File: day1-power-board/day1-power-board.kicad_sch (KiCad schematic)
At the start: 0 parts

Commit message: Complete power supply schematic
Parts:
- added C1: 0.33uF, symbol Device:C
- added C2: 10uF, symbol Device:C
- added C3: 0.1uF, symbol Device:C
- added C4: 33uF, symbol Device:C
- added D1: 1N4007, Diode_THT:D_DO-41_SOD81_P10.16mm_Horizontal, symbol Diode:1N4007
- added D2: LED, symbol Device:LED
- added J1: V_IN, symbol Connector:Screw_Terminal_01x02
- added J2: V_OUT, symbol Connector:Screw_Terminal_01x02
- added R1: 620, symbol Device:R
- added U1: L78L05_SOT89, Package_TO_SOT_SMD:SOT-89-3, symbol Regulator_Linear:L78L05_SOT89
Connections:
- new net: D2.1 (K), R1.1
- new net +5V: C3.1, C4.1, D2.2 (A), J2.1 (Pin_1), U1.1 (OUT)
- new net 12V_PROT: C1.1, C2.1, D1.1 (K), U1.3 (IN)
- new net 12V_RAW: D1.2 (A), J1.2 (Pin_2)
- new net GND: C1.2, C2.2, C3.2, C4.2, J1.1 (Pin_1), J2.2 (Pin_2), R1.2, U1.2 (GND)

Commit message: Complete PCB layout and routing
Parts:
- C1, C2, C3, C4: footprint (none) -> Capacitor_SMD:C_0805_2012Metric
- D2: footprint (none) -> LED_SMD:LED_0603_1608Metric
- J1, J2: footprint (none) -> TerminalBlock_Phoenix:TerminalBlock_Phoenix_MKDS-1,5-2-5.08_1x02_P5.08mm_Horizontal
- R1: footprint (none) -> Resistor_SMD:R_0805_2012Metric
- U1: footprint Package_TO_SOT_SMD:SOT-89-3 -> Package_TO_SOT_THT:TO-220-3_Vertical
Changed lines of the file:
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@@
 			)
 		)
-		(property "Footprint" ""
+		(property "Footprint" "Capacitor_SMD:C_0805_2012Metric"
 			(at 126.6952 82.55 0)
 			(effects
@@
 			)
 		)
-		(property "Footprint" ""
+		(property "Footprint" "TerminalBlock_Phoenix:TerminalBlock_Phoenix_MKDS-1,5-2-5.08_1x02_P5.08mm_Horizontal"
 			(at 223.52 64.77 0)
 			(effects
@@
 			)
 		)
-		(property "Footprint" ""
+		(property "Footprint" "Capacitor_SMD:C_0805_2012Metric"
 			(at 190.1952 83.82 0)
 			(effects
@@
 			)
 		)
-		(property "Footprint" ""
+		(property "Footprint" "Capacitor_SMD:C_0805_2012Metric"
 			(at 173.6852 83.82 0)
 			(effects
@@
 			)
 		)
-		(property "Footprint" ""
+		(property "Footprint" "TerminalBlock_Phoenix:TerminalBlock_Phoenix_MKDS-1,5-2-5.08_1x02_P5.08mm_Horizontal"
 			(at 83.82 67.31 0)
 			(effects
@@
 			)
 		)
-		(property "Footprint" ""
+		(property "Footprint" "Capacitor_SMD:C_0805_2012Metric"
 			(at 141.9352 82.55 0)
 			(effects
@@
 			)
 		)
-		(property "Footprint" ""
+		(property "Footprint" "Resistor_SMD:R_0805_2012Metric"
 			(at 201.422 80.01 90)
 			(effects
@@
 			)
 		)
-		(property "Footprint" ""
+		(property "Footprint" "LED_SMD:LED_0603_1608Metric"
 			(at 203.2 69.85 0)
 			(effects
@@
 			)
 		)
-		(property "Footprint" "Package_TO_SOT_SMD:SOT-89-3"
+		(property "Footprint" "Package_TO_SOT_THT:TO-220-3_Vertical"
 			(at 157.48 59.69 0)
 			(effects

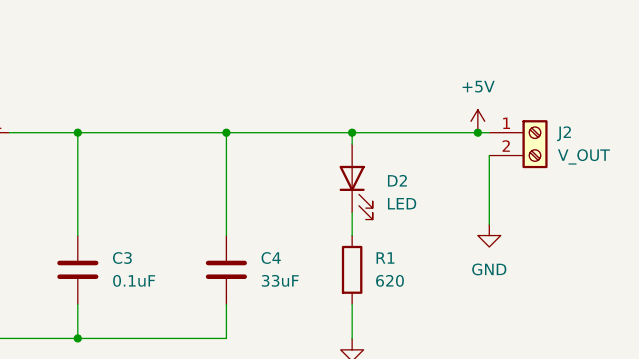
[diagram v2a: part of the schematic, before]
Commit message: Add 5V test point
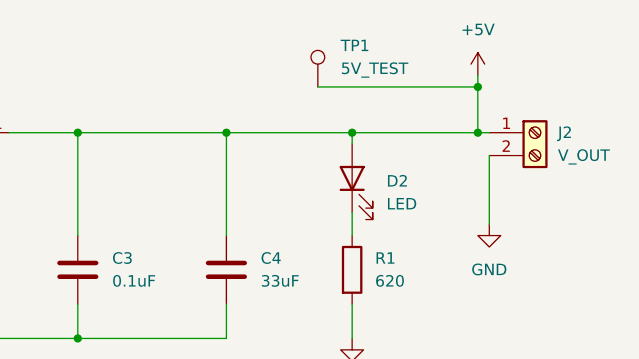
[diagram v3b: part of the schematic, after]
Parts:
- added TP1: 5V_TEST, TestPoint:TestPoint_Pad_2.0x2.0mm, symbol Connector:TestPoint
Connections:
- net +5V: now also TP1.1
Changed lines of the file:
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@@
+	)
+	(junction
+		(at 217.17 59.69)
+		(diameter 0)
+		(color 0 0 0 0)
 	)
 	(junction
@@
 	(wire
 		(pts
+			(xy 199.39 59.69) (xy 217.17 59.69)
+		)
+		(stroke
+			(width 0)
+			(type default)
+		)
+	)
+	(wire
+		(pts
 			(xy 140.97 64.77) (xy 143.51 64.77)
 		)
@@
 	(wire
 		(pts
+			(xy 217.17 59.69) (xy 217.17 64.77)
+		)
+		(stroke
+			(width 0)
+			(type default)
+		)
+	)
+	(wire
+		(pts
 			(xy 172.72 64.77) (xy 172.72 76.2)
 		)
@@
 		(pts
 			(xy 88.9 64.77) (xy 97.79 64.77)
+		)
+		(stroke
+			(width 0)
+			(type default)
+		)
+	)
+	(wire
+		(pts
+			(xy 217.17 58.42) (xy 217.17 59.69)
 		)
 		(stroke
@@
 	)
 	(symbol
+		(lib_id "Connector:TestPoint")
+		(at 199.39 59.69 0)
+		(unit 1)
+		(exclude_from_sim no)
+		(in_bom yes)
+		(on_board yes)
+		(dnp no)
+		(fields_autoplaced yes)
+		(property "Reference" "TP1"
+			(at 201.93 55.1179 0)
+			(effects
+				(font
+					(size 1.27 1.27)
+				)
+				(justify left)
+			)
+		)
+		(property "Value" "5V_TEST"
+			(at 201.93 57.6579 0)
+			(effects
+				(font
+					(size 1.27 1.27)
+				)
+				(justify left)
+			)
+		)
+		(property "Footprint" "TestPoint:TestPoint_Pad_2.0x2.0mm"
+			(at 204.47 59.69 0)
+			(effects
+				(font
+					(size 1.27 1.27)
+				)
+				(hide yes)
+			)
+		)
+		(property "Datasheet" "~"
+			(at 204.47 59.69 0)
+			(effects
+				(font
+					(size 1.27 1.27)
+				)
+				(hide yes)
+			)
+		)
+		(property "Description" "test point"
+			(at 199.39 59.69 0)
+			(effects
+				(font
+					(size 1.27 1.27)
+				)
+				(hide yes)
+			)
+		)
+		(pin "1"
+		)
+		(instances
+			(project ""
+				(path "/36a2fab3-956e-472e-853f-9772f700f857"
+					(reference "TP1")
+					(unit 1)
+				)
+			)
+		)
+	)
+	(symbol
 		(lib_id "Device:C")
 		(at 125.73 78.74 0)
@@
 	(symbol
 		(lib_id "power:+5V")
-		(at 217.17 64.77 0)
+		(at 217.17 58.42 0)
 		(unit 1)
 		(exclude_from_sim no)
@@
 		(fields_autoplaced yes)
 		(property "Reference" "#PWR05"
-			(at 217.17 68.58 0)
+			(at 217.17 62.23 0)
 			(effects
 				(font
@@
 		)
 		(property "Value" "+5V"
-			(at 217.17 59.69 0)
+			(at 217.17 53.34 0)
 			(effects
 				(font
@@
 		)
 		(property "Footprint" ""
-			(at 217.17 64.77 0)
+			(at 217.17 58.42 0)
 			(effects
 				(font
@@
 		)
 		(property "Datasheet" ""
-			(at 217.17 64.77 0)
+			(at 217.17 58.42 0)
 			(effects
 				(font
@@
 		)
 		(property "Description" "Power symbol creates a global label with name \"+5V\""
-			(at 217.17 64.77 0)
-			(effects
-				(font
+			(at 217.17 58.42 0)
+			(effects
+				(font

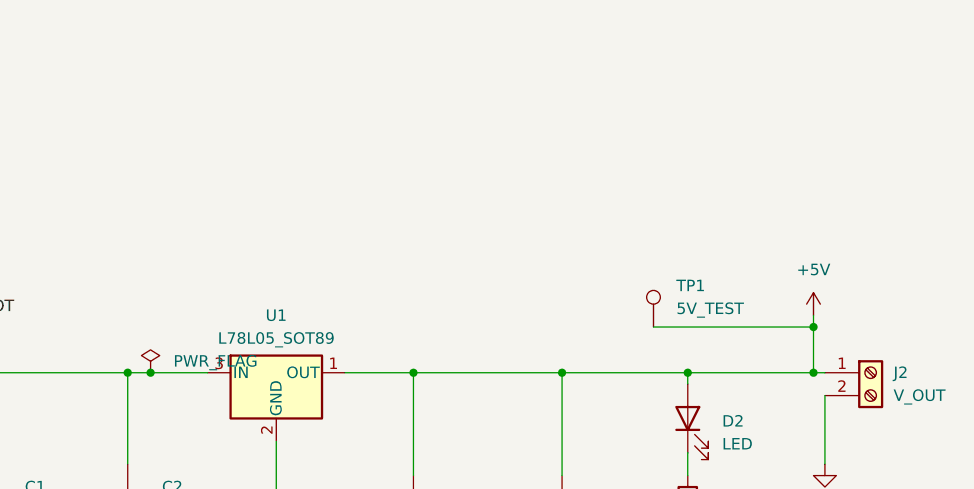
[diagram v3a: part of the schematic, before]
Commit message: Add custom sensor footprint
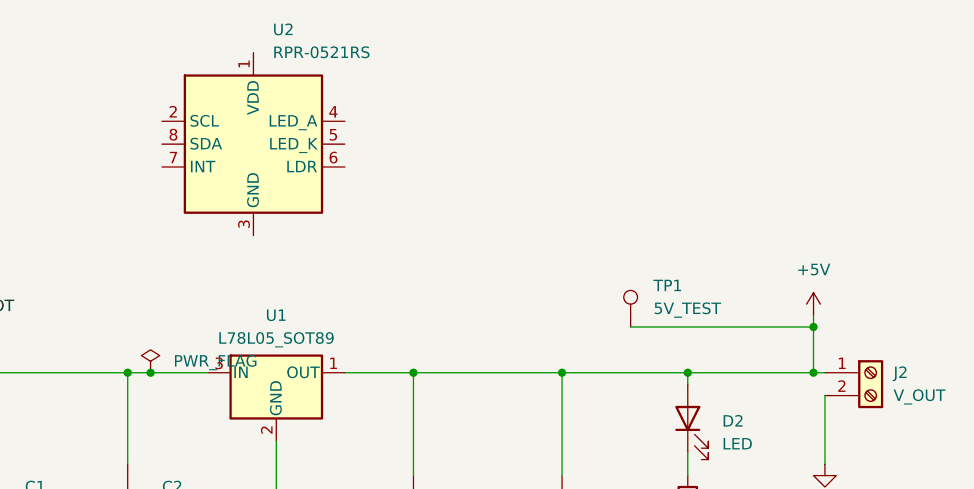
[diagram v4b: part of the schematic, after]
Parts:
- added U2: RPR-0521RS, MYLIBRARY:MY_SENSOR_1x04_P2.54mm, symbol Sensor:RPR-0521RS
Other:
- moved on the sheet: TP1
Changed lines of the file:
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@@
 	(wire
 		(pts
-			(xy 199.39 59.69) (xy 217.17 59.69)
+			(xy 196.85 59.69) (xy 217.17 59.69)
 		)
 		(stroke
@@
 	(symbol
 		(lib_id "Connector:TestPoint")
-		(at 199.39 59.69 0)
+		(at 196.85 59.69 0)
 		(unit 1)
 		(exclude_from_sim no)
@@
 		(fields_autoplaced yes)
 		(property "Reference" "TP1"
-			(at 201.93 55.1179 0)
+			(at 199.39 55.1179 0)
 			(effects
 				(font
@@
 		)
 		(property "Value" "5V_TEST"
-			(at 201.93 57.6579 0)
+			(at 199.39 57.6579 0)
 			(effects
 				(font
@@
 		)
 		(property "Footprint" "TestPoint:TestPoint_Pad_2.0x2.0mm"
-			(at 204.47 59.69 0)
+			(at 201.93 59.69 0)
 			(effects
 				(font
@@
 		)
 		(property "Datasheet" "~"
-			(at 204.47 59.69 0)
+			(at 201.93 59.69 0)
 			(effects
 				(font
@@
 		)
 		(property "Description" "test point"
-			(at 199.39 59.69 0)
+			(at 196.85 59.69 0)
 			(effects
 				(font
@@
 					(unit 1)
 				)
+			)
+		)
+	)
+	(symbol
+		(lib_id "Sensor:RPR-0521RS")
+		(at 154.94 39.37 0)
+		(unit 1)
+		(exclude_from_sim no)
+		(in_bom yes)
+		(on_board yes)
+		(dnp no)
+		(fields_autoplaced yes)
+		(property "Reference" "U2"
+			(at 157.0833 26.67 0)
+			(effects
+				(font
+					(size 1.27 1.27)
+				)
+				(justify left)
+			)
+		)
+		(property "Value" "RPR-0521RS"
+			(at 157.0833 29.21 0)
+			(effects
+				(font
+					(size 1.27 1.27)
+				)
+				(justify left)
+			)
+		)
+		(property "Footprint" "MYLIBRARY:MY_SENSOR_1x04_P2.54mm"
+			(at 154.94 33.401 0)
+			(effects
+				(font
+					(size 1.27 1.27)
+				)
+				(hide yes)
+			)
+		)
+		(property "Datasheet" "https://fscdn.rohm.com/en/products/databook/datasheet/opto/optical_sensor/opto_module/rpr-0521rs-e.pdf"
+			(at 155.067 45.593 0)
+			(effects
+				(font
+					(size 1.27 1.27)
+				)
+				(hide yes)
+			)
+		)
+		(property "Description" "Digital Proximity and Ambient Light Sensor"
+			(at 154.94 39.37 0)
+			(effects
+				(font
+					(size 1.27 1.27)
+				)
+				(hide yes)
+			)
+		)
+		(pin "2"
+		)
+		(pin "4"
+		)
+		(pin "1"
+		)
+		(pin "5"
+		)
+		(pin "7"
+		)
+		(pin "8"
+		)
+		(pin "6"
+		)
+		(pin "3"
+		)
+		(instances
+			(project ""
+				(path "/36a2fab3-956e-472e-853f-9772f700f857"
+					(reference "U2")
+					(unit 1)
+				)

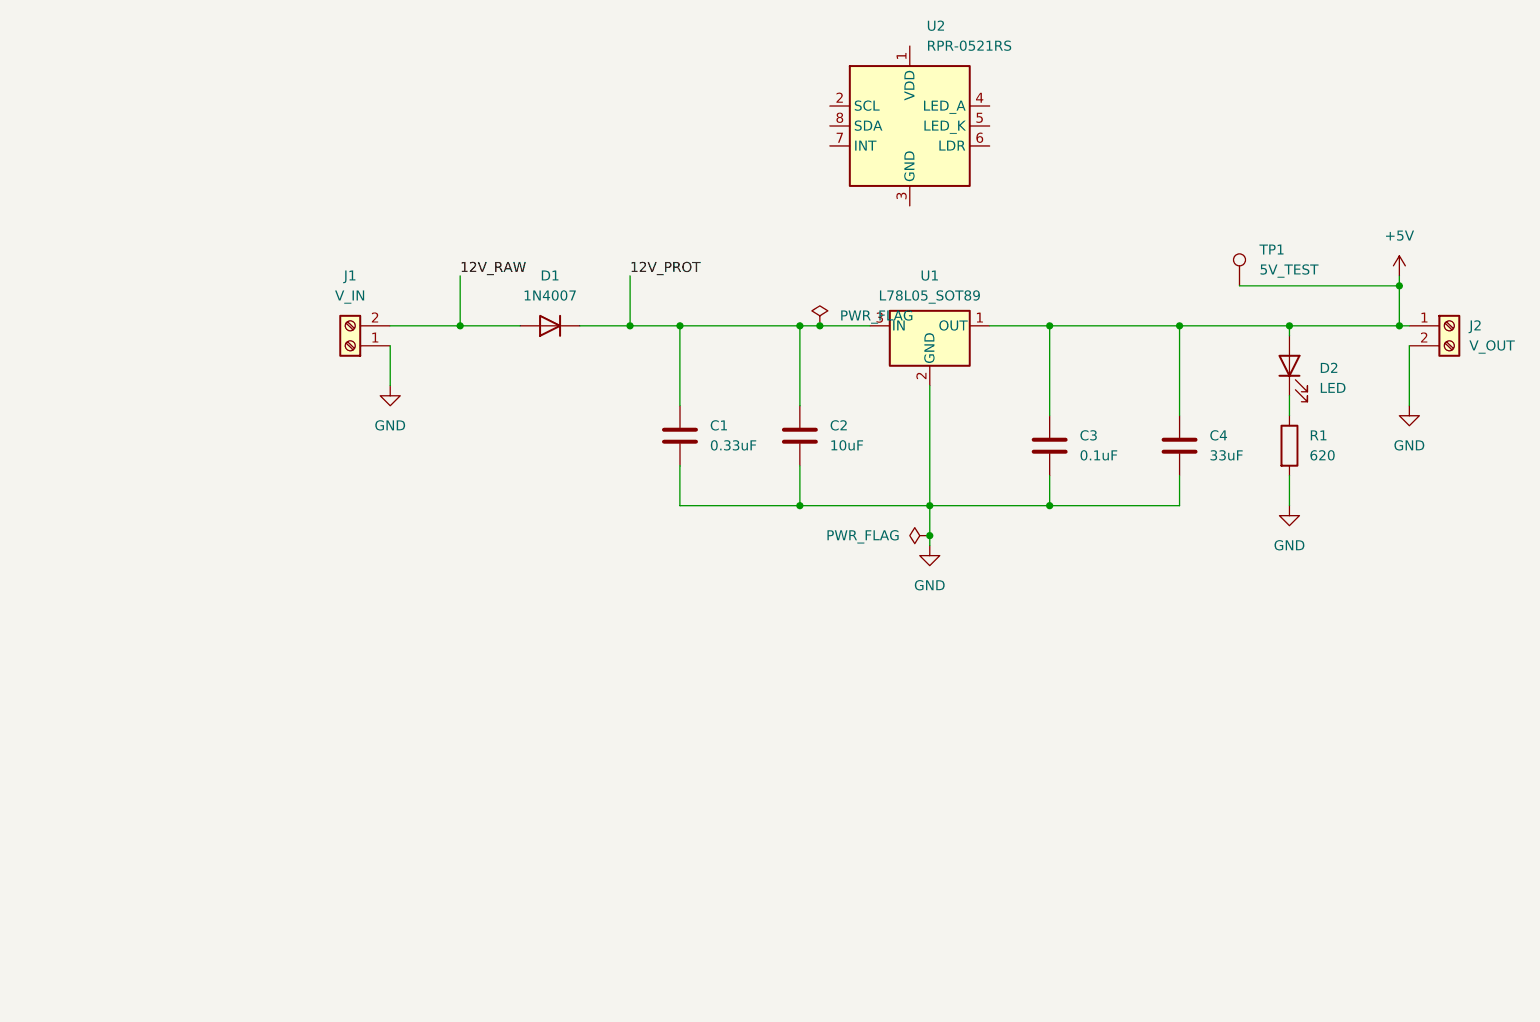
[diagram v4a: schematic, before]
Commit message: Add hierarchical label for power circuit
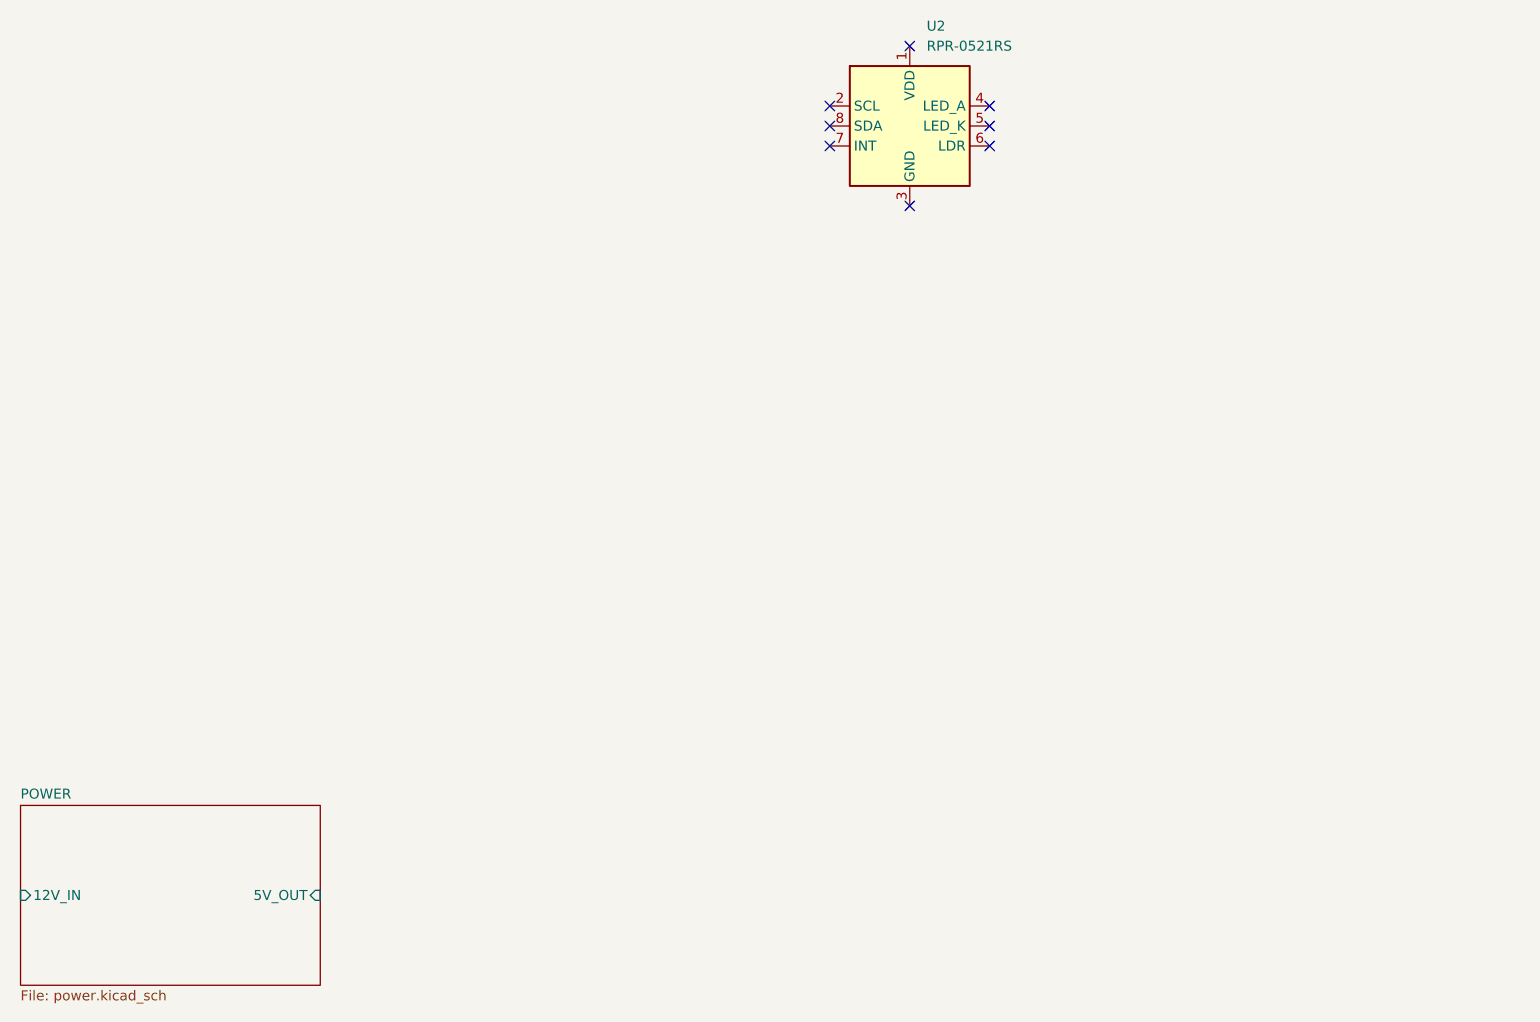
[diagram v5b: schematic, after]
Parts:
- removed C1: 0.33uF, Capacitor_SMD:C_0805_2012Metric, symbol Device:C
- removed C2: 10uF, Capacitor_SMD:C_0805_2012Metric, symbol Device:C
- removed C3: 0.1uF, Capacitor_SMD:C_0805_2012Metric, symbol Device:C
- removed C4: 33uF, Capacitor_SMD:C_0805_2012Metric, symbol Device:C
- removed D1: 1N4007, Diode_THT:D_DO-41_SOD81_P10.16mm_Horizontal, symbol Diode:1N4007
- removed D2: LED, LED_SMD:LED_0603_1608Metric, symbol Device:LED
- removed J1: V_IN, TerminalBlock_Phoenix:TerminalBlock_Phoenix_MKDS-1,5-2-5.08_1x02_P5.08mm_Horizontal, symbol Connector:Screw_Terminal_01x02
- removed J2: V_OUT, TerminalBlock_Phoenix:TerminalBlock_Phoenix_MKDS-1,5-2-5.08_1x02_P5.08mm_Horizontal, symbol Connector:Screw_Terminal_01x02
- removed R1: 620, Resistor_SMD:R_0805_2012Metric, symbol Device:R
- removed TP1: 5V_TEST, TestPoint:TestPoint_Pad_2.0x2.0mm, symbol Connector:TestPoint
- removed U1: L78L05_SOT89, Package_TO_SOT_THT:TO-220-3_Vertical, symbol Regulator_Linear:L78L05_SOT89
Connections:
- no-connect marks 0 -> 8
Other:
- added sheet POWER (power.kicad_sch)

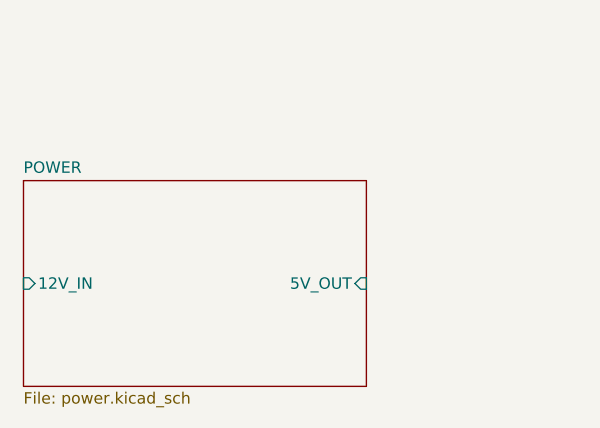
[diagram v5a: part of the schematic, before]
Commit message: Clean up hierarchical schematic
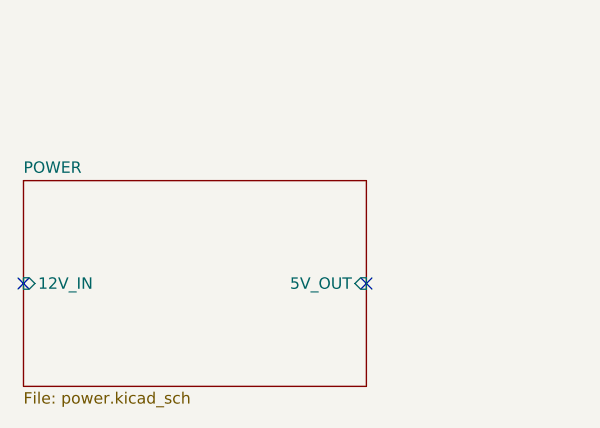
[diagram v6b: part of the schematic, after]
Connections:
- no-connect marks 8 -> 10
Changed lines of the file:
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@@
+	)
+	(no_connect
+		(at 41.91 137.16)
 	)
 	(no_connect
@@
 	)
 	(no_connect
+		(at 80.01 137.16)
+	)
+	(no_connect
